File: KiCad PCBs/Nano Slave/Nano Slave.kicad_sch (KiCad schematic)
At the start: 50 parts, among them J1 Screw_Terminal_01x02, J10 AVR-ISP-6, J11 Conn_01x06_Female, J12 Screw_Terminal_01x02, J13 Screw_Terminal_01x02, J14 Screw_Terminal_01x02, J15 Screw_Terminal_01x02, J16 Screw_Terminal_01x02, J2 Screw_Terminal_01x02, J3 Screw_Terminal_01x02, J4 Screw_Terminal_01x02, J5 Screw_Terminal_01x02, J6 Screw_Terminal_01x02, J7 Screw_Terminal_01x02, J8 Screw_Terminal_01x02, J9 Screw_Terminal_01x02, SW1 SW_DIP_x02, SW2 SW_DIP_x02, SW3 SW_MEC_5E, U1 ATmega328P-AU, U2 MAX487ESA+T, U3 ULN2003A, U5 AMS1117-5.0, Y1 Crystal_GND24

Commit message: Nano Slave Rev 2
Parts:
- added U4: MAX487CPA+, Package_DIP:DIP-8_W7.62mm, symbol A10:MAX487
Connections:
- net +12V: no longer J14.1 (Pin_1)
- net +5V: now also U4.8 (VCC); no longer J15.1 (Pin_1)
- net D2: now also U4.2 (~{RE}), U4.3 (DE)
- net GND: now also J14.1 (Pin_1), J15.1 (Pin_1); no longer J16.1 (Pin_1), J16.2 (Pin_2)
- net RS485+: now also U4.6 (A)
- net RS485-: now also U4.7 (B)
- net RS485_GND: now also U4.5 (GND)
- net RXD: now also U4.1 (RO)
- net TXD: now also U4.4 (DI)
- net A6: now reaches U1.19 (ADC6)
- net A6: now also J16.1 (Pin_1)
- net A7: now reaches U1.22 (ADC7)
- net A7: now also J16.2 (Pin_2)
- no-connect marks 8 -> 6
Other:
- moved on the sheet: J14, J15, J16, J7, J8, J9

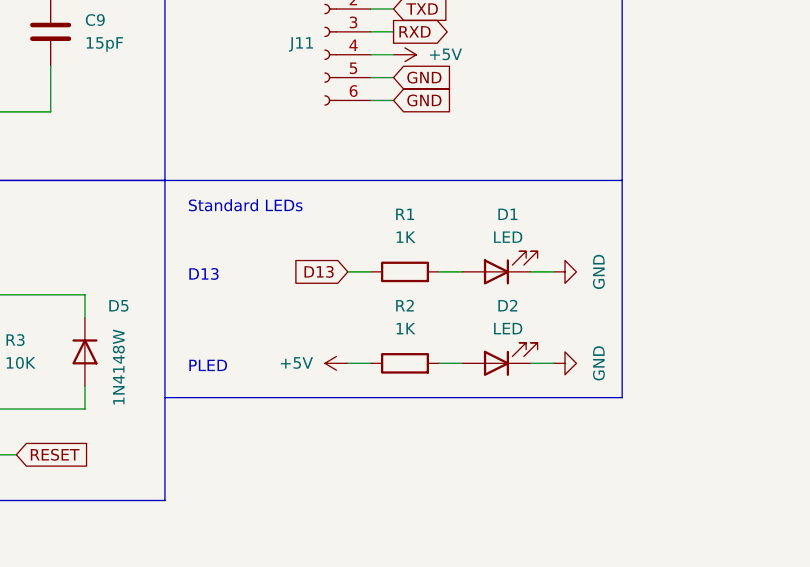
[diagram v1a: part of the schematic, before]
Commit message: Added measurements to silkscreen
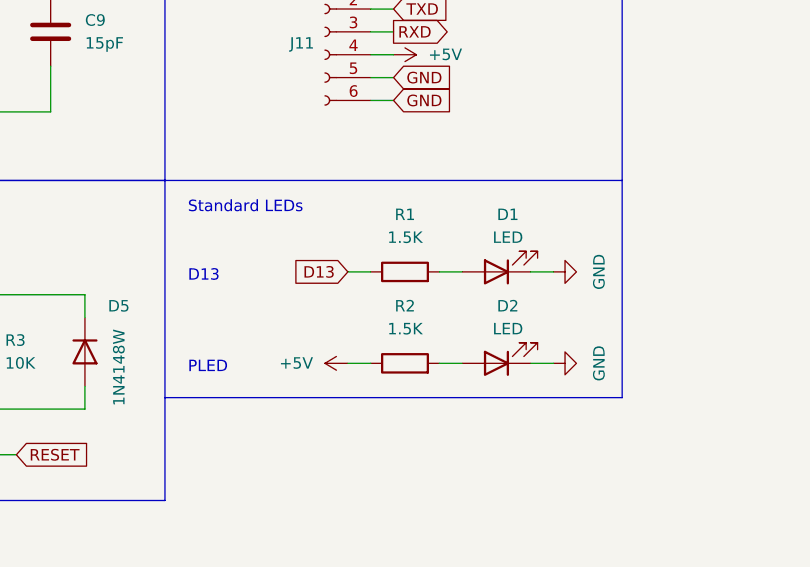
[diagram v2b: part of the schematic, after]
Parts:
- R1, R2: value 1K -> 1.5K; LCSC C17513 -> C4310
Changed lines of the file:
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@@
     (in_bom yes) (on_board yes) (fields_autoplaced)
     (property "Reference" "R1" (id 0) (at 90.17 130.81 90))
-    (property "Value" "1K" (id 1) (at 90.17 133.35 90))
+    (property "Value" "1.5K" (id 1) (at 90.17 133.35 90))
     (property "Footprint" "Resistor_SMD:R_0805_2012Metric" (id 2) (at 90.17 138.938 90)
       (effects (font (size 1.27 1.27)) hide)
@@
       (effects (font (size 1.27 1.27)) hide)
     )
-    (property "LCSC" "C17513" (id 4) (at 90.17 137.16 0)
+    (property "LCSC" "C4310" (id 4) (at 90.17 137.16 0)
       (effects (font (size 1.27 1.27)) hide)
     )
@@
     (in_bom yes) (on_board yes)
     (property "Reference" "R2" (id 0) (at 90.17 140.97 90))
-    (property "Value" "1K" (id 1) (at 90.17 143.51 90))
+    (property "Value" "1.5K" (id 1) (at 90.17 143.51 90))
     (property "Footprint" "Resistor_SMD:R_0805_2012Metric" (id 2) (at 90.17 149.098 90)
       (effects (font (size 1.27 1.27)) hide)
@@
       (effects (font (size 1.27 1.27)) hide)
     )
-    (property "LCSC" "C17513" (id 4) (at 90.17 147.32 0)
+    (property "LCSC" "C4310" (id 4) (at 90.17 147.32 0)
       (effects (font (size 1.27 1.27)) hide)
     )
@@
     )
     (path "/2926a667-ad14-4aa7-a7a2-01eced1fa3d6"
-      (reference "R1") (unit 1) (value "1K") (footprint "Resistor_SMD:R_0805_2012Metric")
+      (reference "R1") (unit 1) (value "1.5K") (footprint "Resistor_SMD:R_0805_2012Metric")
     )
     (path "/bbf61ec7-8a29-4c91-af7f-a22c5fa20a3b"
-      (reference "R2") (unit 1) (value "1K") (footprint "Resistor_SMD:R_0805_2012Metric")
+      (reference "R2") (unit 1) (value "1.5K") (footprint "Resistor_SMD:R_0805_2012Metric")
     )
     (path "/7b18befb-8e40-47a3-8c09-a478787572dc"
